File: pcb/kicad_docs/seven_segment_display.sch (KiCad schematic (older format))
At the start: 21 parts, among them Q1 MMBT3904, Q2 MMBT3904, Q3 MMBT3904, Q4 MMBT3904, U1 HDSP-7503, U2 74HC595, U3 HDSP-7503, U4 HDSP-7503, U5 HDSP-7503

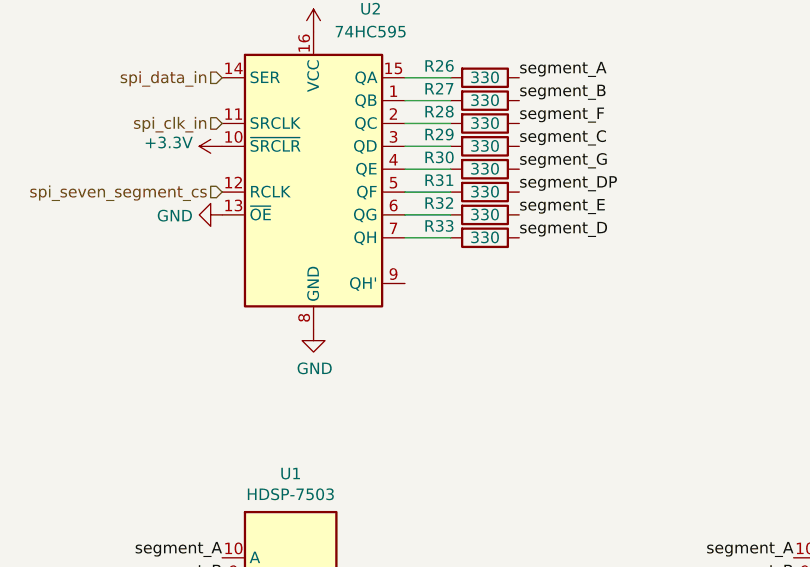
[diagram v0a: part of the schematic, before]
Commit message: add title blocks, fix some erc violations
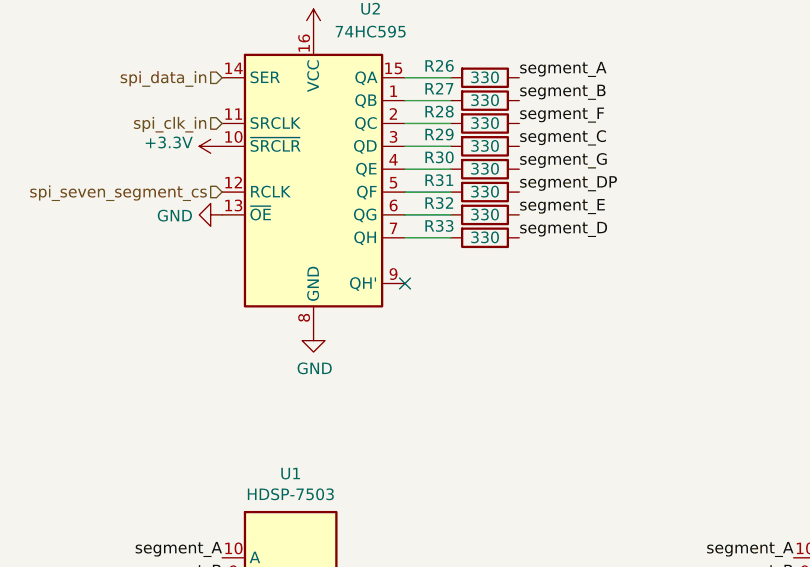
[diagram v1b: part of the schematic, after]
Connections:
- no-connect marks 0 -> 1
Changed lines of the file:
@@
 encoding utf-8
 Sheet 3 10
-Title ""
-Date ""
-Rev ""
+Title "Quad ADSR"
+Date "2020-07-31"
+Rev "0"
 Comp ""
-Comment1 ""
-Comment2 ""
-Comment3 ""
+Comment1 "creativecommons.org/licenses/by/4.0/"
+Comment2 "License: CC by 4.0"
+Comment3 "Author: Jordan Aceto"
 Comment4 ""
 $EndDescr
@@
 Text Label 9400 3700 2    50   ~ 0
 segment_A
+NoConn ~ 2700 2500
 $EndSCHEMATC

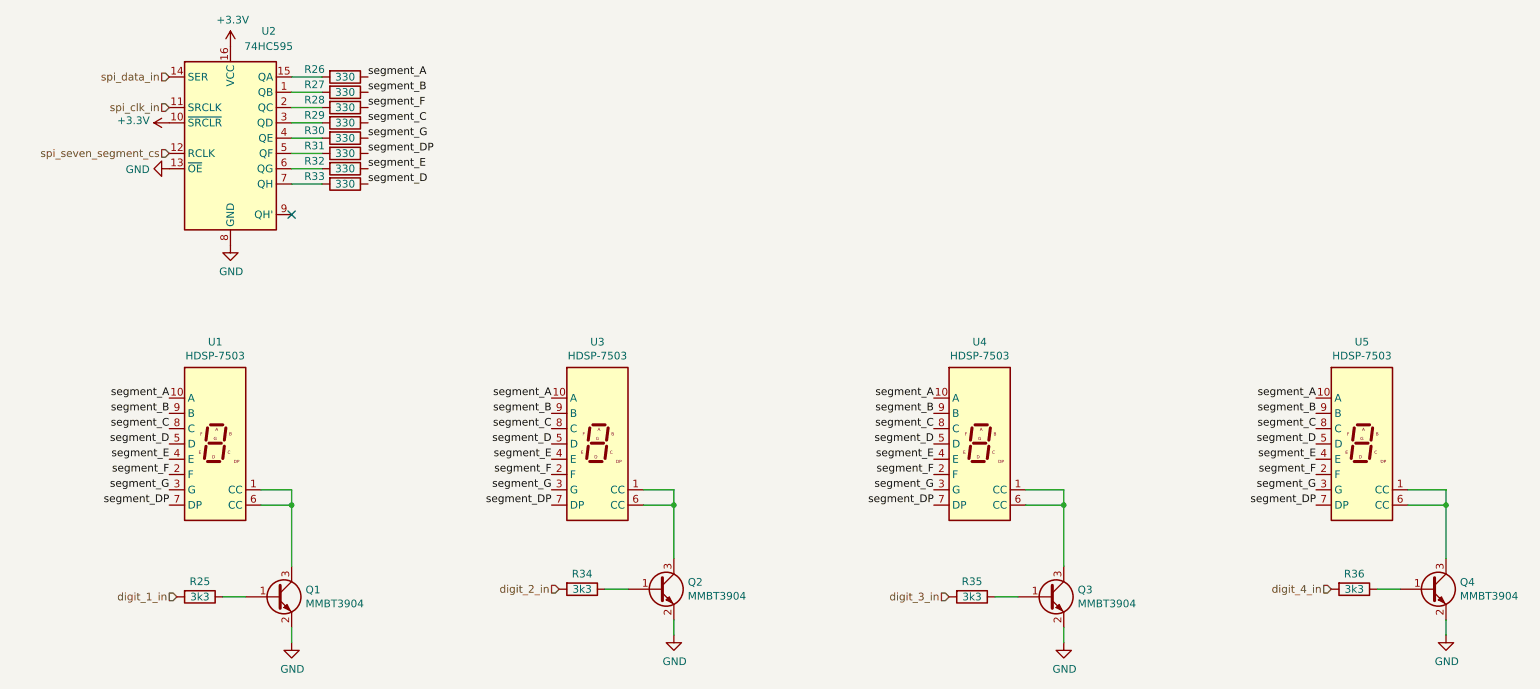
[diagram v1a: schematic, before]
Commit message: change LED current limiting resistors
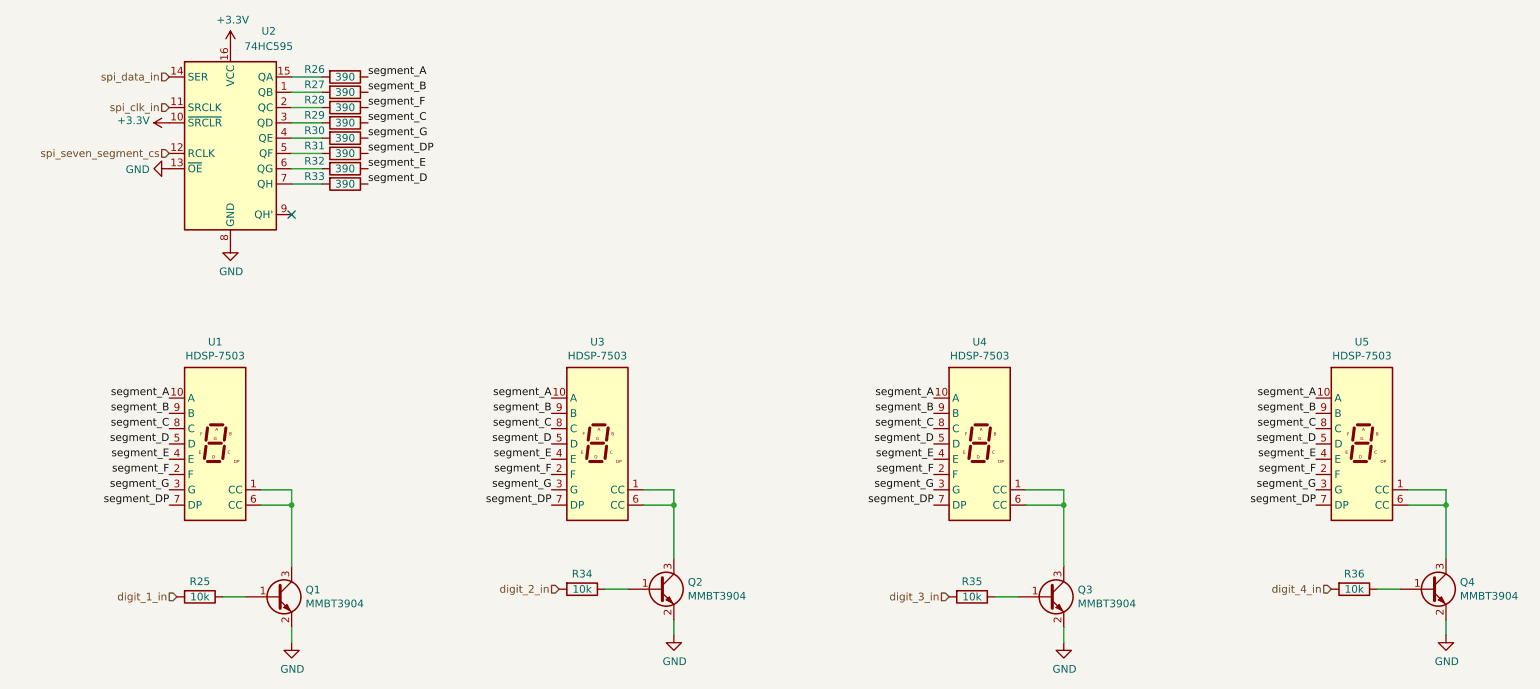
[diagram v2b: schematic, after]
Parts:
- R25, R34, R35, R36: value 3k3 -> 10k
- R26, R27, R28, R29, R30, R31, R32, R33: value 330 -> 390
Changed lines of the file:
@@
 P 2100 5000
 F 0 "R25" V 2000 5000 50  0000 C CNN
-F 1 "3k3" V 2100 5000 50  0000 C CNN
+F 1 "10k" V 2100 5000 50  0000 C CNN
 F 2 "Resistor_SMD:R_0603_1608Metric" V 2030 5000 50  0001 C CNN
 F 3 "~" H 2100 5000 50  0001 C CNN
@@
 P 4600 4950
 F 0 "R34" V 4500 4950 50  0000 C CNN
-F 1 "3k3" V 4600 4950 50  0000 C CNN
+F 1 "10k" V 4600 4950 50  0000 C CNN
 F 2 "Resistor_SMD:R_0603_1608Metric" V 4530 4950 50  0001 C CNN
 F 3 "~" H 4600 4950 50  0001 C CNN
@@
 	1    0    0    -1
 $EndComp
-$Comp
-L Device:R R35
-U 1 1 5E572478
-P 7150 5000
-F 0 "R35" V 7050 5000 50  0000 C CNN
-F 1 "3k3" V 7150 5000 50  0000 C CNN
-F 2 "Resistor_SMD:R_0603_1608Metric" V 7080 5000 50  0001 C CNN
-F 3 "~" H 7150 5000 50  0001 C CNN
-	1    7150 5000
-	0    1    1    0
-$EndComp
 Wire Wire Line
 	7300 5000 7450 5000
@@
 	1    0    0    -1
 $EndComp
-$Comp
-L Device:R R36
-U 1 1 5E5731E6
-P 9650 4950
-F 0 "R36" V 9550 4950 50  0000 C CNN
-F 1 "3k3" V 9650 4950 50  0000 C CNN
-F 2 "Resistor_SMD:R_0603_1608Metric" V 9580 4950 50  0001 C CNN
-F 3 "~" H 9650 4950 50  0001 C CNN
-	1    9650 4950
-	0    1    1    0
-$EndComp
 Wire Wire Line
 	9800 4950 9950 4950
@@
 P 3050 1600
 F 0 "R26" V 3000 1400 50  0000 C CNN
-F 1 "330" V 3050 1600 50  0000 C CNN
+F 1 "390" V 3050 1600 50  0000 C CNN
 F 2 "Resistor_SMD:R_0603_1608Metric" V 2980 1600 50  0001 C CNN
 F 3 "~" H 3050 1600 50  0001 C CNN
@@
 P 3050 1700
 F 0 "R27" V 3000 1500 50  0000 C CNN
-F 1 "330" V 3050 1700 50  0000 C CNN
+F 1 "390" V 3050 1700 50  0000 C CNN
 F 2 "Resistor_SMD:R_0603_1608Metric" V 2980 1700 50  0001 C CNN
 F 3 "~" H 3050 1700 50  0001 C CNN
@@
 P 3050 1800
 F 0 "R28" V 3000 1600 50  0000 C CNN
-F 1 "330" V 3050 1800 50  0000 C CNN
+F 1 "390" V 3050 1800 50  0000 C CNN
 F 2 "Resistor_SMD:R_0603_1608Metric" V 2980 1800 50  0001 C CNN
 F 3 "~" H 3050 1800 50  0001 C CNN
@@
 P 3050 1900
 F 0 "R29" V 3000 1700 50  0000 C CNN
-F 1 "330" V 3050 1900 50  0000 C CNN
+F 1 "390" V 3050 1900 50  0000 C CNN
 F 2 "Resistor_SMD:R_0603_1608Metric" V 2980 1900 50  0001 C CNN
 F 3 "~" H 3050 1900 50  0001 C CNN
@@
 P 3050 2000
 F 0 "R30" V 3000 1800 50  0000 C CNN
-F 1 "330" V 3050 2000 50  0000 C CNN
+F 1 "390" V 3050 2000 50  0000 C CNN
 F 2 "Resistor_SMD:R_0603_1608Metric" V 2980 2000 50  0001 C CNN
 F 3 "~" H 3050 2000 50  0001 C CNN
@@
 P 3050 2100
 F 0 "R31" V 3000 1900 50  0000 C CNN
-F 1 "330" V 3050 2100 50  0000 C CNN
+F 1 "390" V 3050 2100 50  0000 C CNN
 F 2 "Resistor_SMD:R_0603_1608Metric" V 2980 2100 50  0001 C CNN
 F 3 "~" H 3050 2100 50  0001 C CNN
@@
 P 3050 2200
 F 0 "R32" V 3000 2000 50  0000 C CNN
-F 1 "330" V 3050 2200 50  0000 C CNN
+F 1 "390" V 3050 2200 50  0000 C CNN
 F 2 "Resistor_SMD:R_0603_1608Metric" V 2980 2200 50  0001 C CNN
 F 3 "~" H 3050 2200 50  0001 C CNN
@@
 P 3050 2300
 F 0 "R33" V 3000 2100 50  0000 C CNN
-F 1 "330" V 3050 2300 50  0000 C CNN
+F 1 "390" V 3050 2300 50  0000 C CNN
 F 2 "Resistor_SMD:R_0603_1608Metric" V 2980 2300 50  0001 C CNN
 F 3 "~" H 3050 2300 50  0001 C CNN
@@
 segment_A
 NoConn ~ 2700 2500
+$Comp
+L Device:R R36
+U 1 1 5E5731E6
+P 9650 4950
+F 0 "R36" V 9550 4950 50  0000 C CNN
+F 1 "10k" V 9650 4950 50  0000 C CNN
+F 2 "Resistor_SMD:R_0603_1608Metric" V 9580 4950 50  0001 C CNN
+F 3 "~" H 9650 4950 50  0001 C CNN
+	1    9650 4950
+	0    1    1    0
+$EndComp
+$Comp
+L Device:R R35
+U 1 1 5E572478
+P 7150 5000
+F 0 "R35" V 7050 5000 50  0000 C CNN
+F 1 "10k" V 7150 5000 50  0000 C CNN
+F 2 "Resistor_SMD:R_0603_1608Metric" V 7080 5000 50  0001 C CNN
+F 3 "~" H 7150 5000 50  0001 C CNN
+	1    7150 5000
+	0    1    1    0
+$EndComp
 $EndSCHEMATC
